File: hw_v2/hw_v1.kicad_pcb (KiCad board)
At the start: 4 copper layers, 190.1 x 116.5 mm, 501 parts, among them J1 Conn_02x24_Counter_Clockwise, J1 USB_B_Mini, J10 Conn_01x01, J11 Conn_01x01, J12 Conn_01x01, J12 Delphi_Sicma_24, J13 Conn_01x01, J13 Delphi_Sicma_24, J14 Conn_01x04, J15 Conn_01x01, J15 Conn_01x03, J16 47352-1001, J17 Conn_01x01, J19 Conn_01x06, J2 Conn_01x05, J2 Conn_02x05_Odd_Even, J3 Conn_01x01, J3 Conn_01x05, J4 Conn_01x05, J4 Conn_02x05_Counter_Clockwise, J5 Conn_01x01, J5 Conn_01x03, J6 Conn_01x04, J6 Micro_SD_Card_Det, J7 TC2030, J8 USB_B, J9 Tag connect, Q1 AO3400A, Q1 IPD30N06S2L-23, Q2 AO3400A, Q3 FDS6890A, Q4 SS8050, Q5 SS8050, Q6 AO3400A, Q7 AO3400A, SW1 SW_Push, SW2 SW_Push, SW3 SW_Push, SW4 SW_Push, U1 MCZ33810EK, U1 STM32F427VGT6, U10 BMP280, U10 VNLD5090, U11 L78M05ABDT-TR, U12 LM74800, U13 STM32F407VGTx, U14 TJA1051T-3, U15 25Q16, U16 REF3033, U17 SRV05-4, U18 VNLD5090, U19 L78M05ABDT-TR, U2 TC4424A, U2 TLE8888QK, U21 ADXL343, U3 TC4424A, U31 MIC4427, U32 MIC4427, U33 MIC4427, U35 MCP6004, U36 MCP6004, U4 MAX9926UAEE+, U4 TLE9201SG, U46 MCP6004, U5 LM1117-3.3, U5 TPL7407LAPWR, U6 LMV324, U7 LMV324, U7 XC6206 3.3V, U8 AMS1117-3.3, U8 MCP6004, U9 SP720ABTG, U9 VNLD5090, X1 8MHz 20pF, Y1 32.768kHz, Y2 25MHz, Y2 32768 Hz

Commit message: WIP v7
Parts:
- removed the C1 at (87.1, 63.7)
- removed the C1 at (318.1, 78.7)
- removed the C10 at (318.1, 117.7)
- removed the C10 at (49.3, 136.8)
- removed C11, C12, C13, C21, C22, C23: 100nF, Capacitor_SMD:C_0805_2012Metric
- removed C11: 4.7nF, Capacitor_SMD:C_0603_1608Metric
- removed C12: 1nF, Capacitor_SMD:C_0603_1608Metric
- removed C13, C17, C18, C24, C6, C78: 100nF, Capacitor_SMD:C_0603_1608Metric
- removed the C14 at (122.9, 95.6)
- removed the C14 at (325.8, 100.6)
- removed the C15 at (276.8, 63.4)
- removed the C15 at (122.7, 86.3)
- removed C16, C55, C56, C57, C59: 100nF, Capacitor_SMD:C_0402_1005Metric
- removed C16, C17, C18, C24, C27, C28: 0.22uF, Capacitor_SMD:C_0603_1608Metric
- removed the C19 at (105.0, 85.7)
- removed the C19 at (273.4, 63.1)
- removed the C2 at (311.7, 109.6)
- removed the C2 at (90.7, 59.5)
- removed C20: 0.1uF, Capacitor_SMD:C_0805_2012Metric
- removed C20, C79, C80, C82: 10nF, Capacitor_SMD:C_0603_1608Metric
- removed C21, C22: 18pF, Capacitor_SMD:C_0603_1608Metric
- removed C23, C27: 1uF, Capacitor_SMD:C_0603_1608Metric
- removed the C25 at (74.5, 116.7)
- removed the C25 at (298.9, 100.1)
- removed the C26 at (279.7, 96.0)
- removed the C26 at (109.5, 99.1)
- removed C28: 6.8pF, Capacitor_SMD:C_0603_1608Metric
- removed the C29 at (295.9, 117.2)
- removed the C29 at (91.1, 112.3)
- removed the C3 at (87.1, 59.5)
- removed the C3 at (314.3, 78.7)
- removed the C30 at (277.2, 112.6)
- removed the C30 at (115.1, 135.8)
- removed the C31 at (297.6, 112.6)
- removed the C31 at (103.3, 124.2)
- removed the C32 at (297.4, 100.1)
- removed the C32 at (120.6, 116.9)
- removed the C33 at (92.6, 113.8)
- removed the C33 at (279.7, 97.5)
- removed the C34 at (122.9, 126.6)
- removed the C34 at (259.2, 108.6)
- removed the C35 at (308.2, 61.6)
- removed the C35 at (104.9, 128.7)
- removed the C36 at (109.2, 124.8)
- removed the C36 at (261.5, 126.4)
- removed the C37 at (69.2, 81.7)
- removed the C37 at (298.2, 132.6)
- removed the C38 at (261.5, 124.9)
- removed the C38 at (117.9, 105.2)
- removed the C39 at (108.0, 97.6)
- removed the C39 at (260.6, 122.5)
- removed the C4 at (90.7, 63.7)
- removed the C4 at (305.2, 74.9)
- removed the C40 at (299.7, 80.1)
- removed the C40 at (110.8, 123.2)
- removed the C41 at (320.7, 100.6)
- removed the C41 at (112.5, 121.3)
- removed the C42 at (115.3, 115.1)
- removed the C42 at (301.3, 126.1)
- removed the C43 at (326.9, 97.3)
- removed the C43 at (116.7, 116.5)
- removed the C44 at (120.0, 119.0)
- removed the C44 at (283.3, 121.5)
- removed the C45 at (122.9, 124.6)
- removed the C45 at (303.0, 64.7)
- removed the C46 at (118.7, 124.8)
- removed the C46 at (301.1, 63.5)
- removed the C47 at (300.9, 64.7)
- removed the C47 at (96.8, 91.4)
- removed the C48 at (122.7, 99.0)
- removed the C48 at (299.0, 63.5)
- removed the C49 at (122.9, 108.2)
- removed the C49 at (298.5, 64.7)
- removed the C5 at (303.6, 74.9)
- removed the C5 at (85.1, 81.5)
- removed the C50 at (100.7, 89.3)
- removed the C50 at (296.8, 63.5)
- removed the C51 at (296.3, 64.7)
- removed the C51 at (126.4, 58.9)
- removed the C52 at (292.5, 66.7)
- removed the C52 at (130.2, 74.3)
- removed the C53 at (130.3, 59.0)
- removed the C53 at (292.0, 67.9)
- removed the C54 at (290.1, 66.7)
- removed the C54 at (127.8, 79.7)
- removed C55: 100uF ±20% 35V, Capacitor_SMD:CP_Elec_6.3x7.7
- removed C6: 0.01uF, Capacitor_SMD:C_0805_2012Metric
- removed the C7 at (304.3, 77.2)
- removed the C7 at (89.1, 92.8)
- removed the C8 at (318.1, 114.7)
- removed the C8 at (89.1, 95.4)
- removed the C9 at (122.5, 113.4)
- removed the C9 at (318.1, 116.2)
- removed Churrosoft: SYM_Hot_Large, OpenEFI-STM32F_rev3:churro_new_v4
- removed the D1 at (81.4, 53.1)
- removed the D1 at (329.0, 100.9)
- removed the D16 at (105.7, 87.9)
- removed the D16 at (294.7, 132.9)
- removed the D17 at (289.6, 125.6)
- removed the D17 at (113.3, 87.9)
- removed the D19 at (259.2, 107.0)
- removed the D19 at (90.1, 101.9)
- removed the D2 at (81.4, 62.6)
- removed the D2 at (319.5, 106.2)
- removed the D20 at (79.3, 123.8)
- removed the D20 at (322.9, 46.4)
- removed the D21 at (272.5, 117.7)
- removed the D21 at (79.3, 126.8)
- removed the D22 at (84.9, 140.0)
- removed the D22 at (272.5, 119.6)
- removed the D23 at (84.9, 143.2)
- removed the D23 at (272.5, 115.8)
- removed D27: LED-YELLOW, LED_SMD:LED_0805_2012Metric
- removed D27, D31, D32, D33, D34: 3.1v, Diode_SMD:D_SOD-323
- removed the D28 at (74.3, 66.1)
- removed the D28 at (298.2, 95.1)
- removed the D29 at (290.7, 93.7)
- removed the D29 at (49.6, 72.7)
- removed the D3 at (77.5, 44.2)
- removed the D3 at (269.5, 51.8)
- removed the D30 at (52.2, 75.1)
- removed the D30 at (328.4, 76.0)
- removed D31, D33, D35: LED-RED, LED_SMD:LED_0603_1608Metric
- removed D32, D34, D43: 1N4148WS, Diode_SMD:D_SOD-323
- removed D35: SM6T33A, Diode_SMD:D_SMB
- removed D36: SS54, Diode_SMD:D_SMA
- removed D38, D39, D40: SRV05-4, Package_TO_SOT_SMD:SOT-23-6
- removed the D4 at (81.4, 50.9)
- removed the D4 at (275.1, 51.9)
- removed D41: SM15T33C, Diode_SMD:D_SMC
- removed D42: BAV70, Package_TO_SOT_SMD:SOT-23
- removed the D5 at (81.4, 60.5)
- removed the D5 at (269.5, 48.2)
- removed the D6 at (77.5, 42.2)
- removed the D6 at (269.5, 44.7)
- removed the D7 at (81.4, 58.4)
- removed the D7 at (288.3, 129.1)
- removed F1: Polyfuse, Fuse:Fuse_1812_4532Metric
- removed FB1: FILTER, Resistor_SMD:R_0603_1608Metric_Pad1.05x0.95mm_HandSolder
- removed FID3, FID4, FID5, FID6: Fiducial, Fiducial:Fiducial_0.5mm_Mask1mm
- removed the G*** at (62.8, 113.8)
- removed the G*** at (96.8, 136.5)
- removed the J1 at (185.2, 125.3)
- removed J12: Delphi_Sicma_24, uEFI_v5:Delphi_Sicma_24_Grey
- removed J12, J13, J15 (x2), J17, J5: Conn_01x01, Connector_Pin:Pin_D0.7mm_L6.5mm_W1.8mm_FlatFork
- removed J13: Delphi_Sicma_24, uEFI_v5:Delphi_Sicma_24_Black
- removed J15, J5: Conn_01x03, Connector_PinHeader_2.54mm:PinHeader_1x03_P2.54mm_Vertical
- removed J19: Conn_01x06, Connector_JST:JST_EH_B5B-EH-A_1x05_P2.50mm_Vertical
- removed the J2 at (280.0, 129.6)
- removed the J2 at (39.2, 99.0)
- removed the J3 at (275.1, 57.0)
- removed the J3 at (86.0, 43.3)
- removed J4: Conn_01x05, Connector_PinHeader_2.54mm:PinHeader_1x05_P2.54mm_Vertical
- removed J4: Conn_02x05_Counter_Clockwise, Connector_PinHeader_2.54mm:PinHeader_2x05_P2.54mm_Vertical_SMD
- removed J6: Micro_SD_Card_Det, Connector_Card:microSD_HC_Molex_104031-0811
- removed J6: Conn_01x04, Connector_PinHeader_2.54mm:PinHeader_1x04_P2.54mm_Vertical
- removed J7: TC2030, Connector:Tag-Connect_TC2030-IDC-NL_2x03_P1.27mm_Vertical
- removed JP1: Jumper_3_Bridged12, Jumper:SolderJumper-3_P1.3mm_Bridged12_Pad1.0x1.5mm
- removed JP14: Jumper_2_Open, Jumper:SolderJumper-2_P1.3mm_Open_TrianglePad1.0x1.5mm
- removed the JP2 at (279.6, 82.2)
- removed the JP2 at (84.4, 69.1)
- removed JP4: SolderJumper_2_Open, Jumper:SolderJumper-2_P1.3mm_Open_RoundedPad1.0x1.5mm
- removed LOGO1: DNP, Symbol:OSHW-Logo2_7.3x6mm_SilkScreen
- removed LOGO3: LOGO, rusefi_lib:MRE_QR_code
- removed NT1: Net-Tie_2, rusEFI_Ola:Net-Tie_2_8.5mil
- removed NT2: Net-Tie_2, hw_microRusEfi-master:Net-Tie_2_8.5mil
- removed NT3: Analog Ground Net Tie, NetTie:NetTie-2_SMD_Pad0.5mm
- removed Q1: IPD30N06S2L-23, Package_TO_SOT_SMD:TO-252-2
- removed Q1, Q2: AO3400A, Package_TO_SOT_SMD:SOT-23
- removed Q3: FDS6890A, Package_SO:SOP-8_3.9x4.9mm_P1.27mm
- removed the R1 at (41.7, 66.3)
- removed the R1 at (273.9, 76.0)
- removed R10, R5: 10k, Resistor_SMD:R_0603_1608Metric
- removed R10: 1k, Resistor_SMD:R_1206_3216Metric
- removed the R11 at (287.4, 65.7)
- removed the R11 at (78.1, 83.5)
- removed R12, R13, R141, R39, R45, R46, R6, R60, R61, R62, R63, R70, R71, R76, R77, R78: 10K, Resistor_SMD:R_0603_1608Metric
- removed R12, R13, R18, R19, R20, R28, R29, R30: 470R, Resistor_SMD:R_0805_2012Metric
- removed R120, R121, R122, R123, R124, R125: 100, Resistor_SMD:R_1206_3216Metric
- removed R131, R24, R41, R52: 470K, Resistor_SMD:R_0402_1005Metric
- removed R139: 39k, Resistor_SMD:R_0603_1608Metric
- removed R14, R20, R23, R25: 2.7k, Resistor_SMD:R_0603_1608Metric
- removed R14, R15, R25: 2.49k +-1%, Resistor_SMD:R_0603_1608Metric
- removed R15, R17, R18, R19: DNP, Resistor_SMD:R_0603_1608Metric
- removed the R16 at (272.4, 76.0)
- removed the R16 at (74.5, 114.6)
- removed R17, R24, R33, R35, R36, R45, R46, R47: 180k, Resistor_SMD:R_0805_2012Metric
- removed the R2 at (308.9, 102.0)
- removed the R2 at (90.7, 57.4)
- removed R21: 604R, Resistor_SMD:R_0805_2012Metric
- removed R21, R30, R33, R8, R84, R85: 0R, Resistor_SMD:R_0603_1608Metric
- removed R22: 3.88k, Resistor_SMD:R_0603_1608Metric
- removed R22: 120, Resistor_SMD:R_0805_2012Metric
- removed R23, R26, R39, R40, R41, R50, R51, R52: 348k, Resistor_SMD:R_0805_2012Metric
- removed R26, R35, R5, R59, R64, R65, R66, R67, R72, R73, R74: 6.8K, Resistor_SMD:R_0603_1608Metric
- removed the R27 at (98.7, 121.3)
- removed the R27 at (288.1, 63.0)
- removed R28, R48: 2.2k, Resistor_SMD:R_0603_1608Metric
- removed R29, R36, R48, R49 (x2), R50, R51, R59, R6, R60, R61, R66, R9: 1k, Resistor_SMD:R_0603_1608Metric
- removed the R3 at (87.1, 61.6)
- removed the R3 at (307.2, 80.4)
- removed the R31 at (116.4, 48.5)
- removed the R31 at (297.3, 51.5)
- removed the R32 at (293.2, 88.1)
- removed the R32 at (87.5, 123.9)
- removed the R34 at (297.0, 56.5)
- removed the R34 at (87.5, 127.0)
- removed the R37 at (87.7, 135.6)
- removed the R37 at (296.6, 54.1)
- removed the R38 at (296.2, 91.1)
- removed the R38 at (89.4, 135.6)
- removed the R4 at (307.6, 97.4)
- removed the R4 at (90.7, 61.6)
- removed R40: DNP, Resistor_SMD:R_0402_1005Metric
- removed the R42 at (83.0, 130.1)
- removed the R42 at (273.4, 61.6)
- removed the R43 at (83.0, 132.9)
- removed the R43 at (271.0, 130.5)
- removed the R44 at (293.2, 91.1)
- removed the R44 at (83.0, 135.7)
- removed R47: 100K, Resistor_SMD:R_0603_1608Metric
- removed the R53 at (74.6, 69.6)
- removed the R53 at (302.2, 88.1)
- removed the R54 at (77.4, 62.7)
- removed the R54 at (302.8, 56.8)
- removed the R55 at (300.7, 88.1)
- removed the R55 at (54.8, 83.7)
- removed the R56 at (299.2, 51.5)
- removed the R56 at (54.8, 77.9)
- removed the R57 at (299.2, 88.1)
- removed the R57 at (54.8, 79.9)
- removed the R58 at (54.8, 82.0)
- removed the R58 at (299.5, 56.5)
- removed R62: 48.7k, Resistor_SMD:R_0603_1608Metric
- removed R63: 42.2k, Resistor_SMD:R_0603_1608Metric
- removed R64: 9.09k, Resistor_SMD:R_0603_1608Metric
- removed R65: 3.48k, Resistor_SMD:R_0603_1608Metric
- removed R67: 100R, Resistor_SMD:R_0603_1608Metric
- removed the R68 at (290.2, 91.1)
- removed the R68 at (93.0, 36.1)
- removed the R69 at (93.0, 39.2)
- removed the R69 at (288.7, 91.1)
- removed the R7 at (304.6, 59.4)
- removed the R7 at (85.1, 78.0)
- removed R8: 4.99K 1/2W, Resistor_SMD:R_0805_2012Metric
- removed R83, R9: 4.7K, Resistor_SMD:R_0603_1608Metric
- removed R86: 0R, Resistor_SMD:R_0805_2012Metric
- removed REF** (x4): MountingHole_3.2mm_M3_ISO14580_Pad, MountingHole:MountingHole_3.2mm_M3_ISO14580_Pad
- removed the RN1 at (77.7, 51.5)
- removed the RN1 at (268.9, 116.3)
- removed RN13: 10k, Resistor_SMD:R_Array_Convex_4x0603
- removed the RN2 at (77.5, 59.4)
- removed the RN2 at (302.1, 60.8)
- removed the RN3 at (101.2, 128.0)
- removed the RN3 at (291.5, 63.6)
- removed SW1: SW_Push, Button_Switch_SMD:SW_SPST_CK_RS282G05A3
- removed the SW2 at (118.5, 140.0)
- removed the SW2 at (270.5, 104.8)
- removed SW3, SW4: SW_Push, Button_Switch_SMD:SW_Push_SPST_NO_Alps_SKRK
- removed TP0: GND, TestPoint:TestPoint_Pad_D2.0mm
- removed the TP1 at (90.5, 57.4)
- removed the TP1 at (281.7, 87.9)
- removed TP10, TP11, TP14, TP15, TP16, TP17, TP18, TP19, TP20, TP9: TestPoint_Alt, TestPoint:TestPoint_THTPad_1.0x1.0mm_Drill0.5mm
- removed the TP12 at (258.4, 91.8)
- removed the TP12 at (73.2, 84.6)
- removed the TP2 at (287.6, 94.9)
- removed the TP2 at (83.3, 90.5)
- removed the TP3 at (258.4, 100.9)
- removed the TP3 at (88.0, 84.6)
- removed the TP4 at (301.3, 94.3)
- removed the TP4 at (83.2, 86.1)
- removed the TP5 at (258.4, 97.9)
- removed the TP5 at (79.6, 85.3)
- removed U1: STM32F427VGT6, Package_QFP:LQFP-100_14x14mm_P0.5mm
- removed U1: MCZ33810EK, uEFI_v5:SOP65P1030X245-33N
- removed the U10 at (319.9, 71.0)
- removed the U10 at (100.8, 86.0)
- removed the U2 at (317.3, 89.1)
- removed U31, U32, U33: MIC4427, Package_SO:SOIC-8_3.9x4.9mm_P1.27mm
- removed U35, U36, U46: MCP6004, Package_SO:TSSOP-14_4.4x5mm_P0.65mm
- removed U4: MAX9926UAEE+, Package_SO:QSOP-16_3.9x4.9mm_P0.635mm
- removed U4: TLE9201SG, Package_SO:Infineon_PG-DSO-12-11
- removed the U5 at (261.4, 116.6)
- removed the U5 at (64.6, 70.6)
- removed the U7 at (304.7, 113.0)
- removed the U7 at (98.5, 79.3)
- removed the U8 at (298.6, 83.7)
- removed the U8 at (128.1, 114.4)
- removed the U9 at (98.6, 62.5)
- removed the U9 at (314.3, 71.0)
- removed X1: 8MHz 20pF, Crystal:Crystal_SMD_5032-2Pin_5.0x3.2mm
- removed the Y2 at (114.9, 119.7)
- removed the Y2 at (282.1, 118.8)
- added C1: 0.01uF, Capacitor_SMD:C_0805_2012Metric, F.Cu at (223.8, 129.2)
- added C10: 100uF ±20% 35V, Capacitor_SMD:CP_Elec_6.3x7.7, F.Cu at (226.7, 91.4)
- added C14: 100nF, Capacitor_SMD:C_0805_2012Metric, F.Cu at (210.3, 105.7)
- added C15: 47nF, Capacitor_SMD:C_0603_1608Metric, F.Cu at (201.5, 102.4)
- added C19: 100nF, Capacitor_SMD:C_0402_1005Metric, F.Cu at (239.8, 102.2)
- added C2: 0.01uF, Capacitor_SMD:C_0805_2012Metric, F.Cu at (223.8, 132.2)
- added C25: 100nF, Capacitor_SMD:C_0402_1005Metric, F.Cu at (239.8, 104.1)
- added C26: 2.2uF, Capacitor_SMD:C_0805_2012Metric, F.Cu at (194.0, 66.9)
- added C29: 2.2uF, Capacitor_SMD:C_0805_2012Metric, F.Cu at (194.0, 69.9)
- added C3: 10nF, Capacitor_SMD:C_0603_1608Metric, F.Cu at (219.6, 128.9)
- added C30: 100nF, Capacitor_SMD:C_0805_2012Metric, F.Cu at (194.0, 73.0)
- added C31: 100nF, Capacitor_SMD:C_0805_2012Metric, F.Cu at (194.0, 76.0)
- added C32: 100nF, Capacitor_SMD:C_0805_2012Metric, F.Cu at (194.0, 79.0)
- added C33: 100nF, Capacitor_SMD:C_0805_2012Metric, F.Cu at (194.0, 82.0)
- added C34: 1uF, Capacitor_SMD:C_0805_2012Metric, F.Cu at (194.0, 85.0)
- added C35: 100nF, Capacitor_SMD:C_0805_2012Metric, F.Cu at (198.4, 66.9)
- added C36: 100nF, Capacitor_SMD:C_0805_2012Metric, F.Cu at (198.4, 69.9)
- added C37: 100nF, Capacitor_SMD:C_0805_2012Metric, F.Cu at (198.4, 73.0)
- added C38: 4.7uF, Capacitor_SMD:C_0805_2012Metric, F.Cu at (198.4, 76.0)
- added C39: 100nF, Capacitor_SMD:C_0805_2012Metric, F.Cu at (198.4, 79.0)
- added C4: 10nF, Capacitor_SMD:C_0603_1608Metric, F.Cu at (219.6, 131.4)
- added C40: 6.8pF, Capacitor_SMD:C_0805_2012Metric, F.Cu at (198.4, 82.0)
- added C41: 6.8pF, Capacitor_SMD:C_0805_2012Metric, F.Cu at (198.4, 85.0)
- added C42: 15pF, Capacitor_SMD:C_0805_2012Metric, F.Cu at (202.9, 66.9)
- added C43: 15pF, Capacitor_SMD:C_0805_2012Metric, F.Cu at (202.9, 69.9)
- added C44: 1u, Capacitor_SMD:C_0805_2012Metric, F.Cu at (202.9, 73.0)
- added C45: 1u, Capacitor_SMD:C_0805_2012Metric, F.Cu at (202.9, 76.0)
- added C46: 100n, Capacitor_SMD:C_0805_2012Metric, F.Cu at (202.9, 79.0)
- added C47: 100nF, Capacitor_SMD:C_0805_2012Metric, F.Cu at (224.4, 120.2)
- added C48: 47nF, Capacitor_SMD:C_0603_1608Metric, F.Cu at (201.5, 104.9)
- added C49: 100nF, Capacitor_SMD:C_0805_2012Metric, F.Cu at (210.3, 108.7)
- added C5: 0.01uF, Capacitor_SMD:C_0805_2012Metric, F.Cu at (223.8, 135.2)
- added C50: 100nF, Capacitor_SMD:C_0805_2012Metric, F.Cu at (224.4, 123.3)
- added C51: 10nF, Capacitor_SMD:C_0603_1608Metric, F.Cu at (201.5, 107.5)
- added C52: 10nF, Capacitor_SMD:C_0603_1608Metric, F.Cu at (201.5, 110.0)
- added C53: 10nF, Capacitor_SMD:C_0603_1608Metric, F.Cu at (201.5, 112.5)
- added C54: 10nF, Capacitor_SMD:C_0603_1608Metric, F.Cu at (201.5, 115.0)
- added C60: 100nF, Capacitor_SMD:C_0402_1005Metric, F.Cu at (239.8, 108.1)
- added C63: 10nF, Capacitor_SMD:C_0603_1608Metric, F.Cu at (219.6, 102.4)
- added C64: 100nF, Capacitor_SMD:C_0402_1005Metric, F.Cu at (239.8, 110.0)
- added C66: 100nF, Capacitor_SMD:C_0402_1005Metric, F.Cu at (239.8, 112.0)
- added C68: 10nF, Capacitor_SMD:C_0603_1608Metric, F.Cu at (219.6, 104.9)
- added C69: 100uF ±20% 35V, Capacitor_SMD:CP_Elec_6.3x7.7, F.Cu at (204.7, 128.1)
- added C7: 0.01uF, Capacitor_SMD:C_0805_2012Metric, F.Cu at (223.8, 138.2)
- added C8: 4.7nF, Capacitor_SMD:C_0805_2012Metric, F.Cu at (223.8, 141.2)
- added C9: 100nF, Capacitor_SMD:C_0805_2012Metric, F.Cu at (210.3, 102.7)
- added D1: LED, LED_SMD:LED_0805_2012Metric, F.Cu at (249.8, 102.7)
- added D16: SRV05-4, Package_TO_SOT_SMD:SOT-23-6, F.Cu at (240.6, 121.3)
- added D17: SS54, Diode_SMD:D_SMA, F.Cu at (191.4, 128.2)
- added D19: 1N5819WS, Diode_SMD:D_SOD-323_HandSoldering, F.Cu at (197.4, 97.5)
- added D2: LED, LED_SMD:LED_0805_2012Metric, F.Cu at (249.8, 105.7)
- added D20: LED, LED_SMD:LED_0805_2012Metric, F.Cu at (189.5, 66.9)
- added D21: LED, LED_SMD:LED_0805_2012Metric, F.Cu at (189.5, 70.0)
- added D22: LED, LED_SMD:LED_0805_2012Metric, F.Cu at (189.5, 73.0)
- added D23: LED, LED_SMD:LED_0805_2012Metric, F.Cu at (189.5, 76.1)
- added D28: MM3Z24VT1G, Diode_SMD:D_SOD-323, F.Cu at (234.1, 95.5)
- added D29: S110FA, Diode_SMD:D_SOD-123F, F.Cu at (234.7, 89.0)
- added D3: 1N5819WS, Diode_SMD:D_SOD-323_HandSoldering, F.Cu at (263.0, 102.7)
- added D30: S110FA, Diode_SMD:D_SOD-123F, F.Cu at (234.7, 92.3)
- added D4: LED, LED_SMD:LED_0805_2012Metric, F.Cu at (249.8, 108.8)
- added D5: LED, LED_SMD:LED_0805_2012Metric, F.Cu at (249.8, 111.8)
- added D6: 1N5819WS, Diode_SMD:D_SOD-323_HandSoldering, F.Cu at (263.0, 105.6)
- added D7: LED, LED_SMD:LED_0805_2012Metric, F.Cu at (249.8, 114.9)
- added FID2: Fiducial, Fiducial:Fiducial_0.5mm_Mask1mm, F.Cu at (227.9, 122.6)
- added J2: Conn_01x01, TestPoint:TestPoint_THTPad_2.0x2.0mm_Drill1.0mm, F.Cu at (249.2, 67.5)
- added J3: Conn_01x01, TestPoint:TestPoint_THTPad_2.0x2.0mm_Drill1.0mm, F.Cu at (249.2, 71.5)
- added JP2: Jumper_3_Bridged12, Jumper:SolderJumper-3_P1.3mm_Bridged12_Pad1.0x1.5mm, F.Cu at (233.1, 140.1)
- added R1: 2.2k, Resistor_SMD:R_0603_1608Metric, F.Cu at (219.6, 133.9)
- added R100: 10K, Resistor_SMD:R_0603_1608Metric, F.Cu at (223.6, 115.0)
- added R101: 39k, Resistor_SMD:R_0603_1608Metric, F.Cu at (223.6, 117.5)
- added R102: 6.8K, Resistor_SMD:R_0603_1608Metric, F.Cu at (227.6, 102.4)
- added R104: 6.8K, Resistor_SMD:R_0603_1608Metric, F.Cu at (227.6, 104.9)
- added R106: 10K, Resistor_SMD:R_0603_1608Metric, F.Cu at (227.6, 107.5)
- added R108: 10K, Resistor_SMD:R_0603_1608Metric, F.Cu at (227.6, 110.0)
- added R11: 10k, Resistor_SMD:R_0603_1608Metric, F.Cu at (219.6, 144.0)
- added R16: 2.7k, Resistor_SMD:R_0603_1608Metric, F.Cu at (219.6, 107.5)
- added R2: 10k, Resistor_SMD:R_0603_1608Metric, F.Cu at (219.6, 136.4)
- added R27: 10k, Resistor_SMD:R_0603_1608Metric, F.Cu at (207.1, 66.7)
- added R3: 10k, Resistor_SMD:R_0603_1608Metric, F.Cu at (219.6, 138.9)
- added R31: 120R, Resistor_SMD:R_1206_3216Metric, F.Cu at (207.9, 96.7)
- added R32: 4.7k, Resistor_SMD:R_0603_1608Metric, F.Cu at (207.1, 69.2)
- added R34: 4.7k, Resistor_SMD:R_0603_1608Metric, F.Cu at (207.1, 71.7)
- added R37: 4.7k, Resistor_SMD:R_0603_1608Metric, F.Cu at (207.1, 74.2)
- added R38: 4.7k, Resistor_SMD:R_0603_1608Metric, F.Cu at (207.1, 76.7)
- added R4: 2.2k, Resistor_SMD:R_0603_1608Metric, F.Cu at (219.6, 141.5)
- added R42: 4.7k, Resistor_SMD:R_0603_1608Metric, F.Cu at (207.1, 79.2)
- added R43: 4.7k, Resistor_SMD:R_0603_1608Metric, F.Cu at (207.1, 81.7)
- added R44: 4.7k, Resistor_SMD:R_0603_1608Metric, F.Cu at (207.1, 84.2)
- added R53: 1k, Resistor_SMD:R_0603_1608Metric, F.Cu at (240.3, 66.7)
- added R54: 100k, Resistor_SMD:R_0603_1608Metric, F.Cu at (240.3, 69.2)
- added R55: 100k, Resistor_SMD:R_0603_1608Metric, F.Cu at (240.3, 71.7)
- added R56: 100k, Resistor_SMD:R_0603_1608Metric, F.Cu at (240.3, 74.2)
- added R57: 1k, Resistor_SMD:R_0603_1608Metric, F.Cu at (240.3, 76.7)
- added R58: 1k, Resistor_SMD:R_0603_1608Metric, F.Cu at (240.3, 79.2)
- added R68: 1k, Resistor_SMD:R_0603_1608Metric, F.Cu at (240.3, 81.7)
- added R69: 100k, Resistor_SMD:R_0603_1608Metric, F.Cu at (240.3, 84.2)
- added R7: 4.99K 1/2W, Resistor_SMD:R_0805_2012Metric, F.Cu at (232.5, 143.6)
- added R91: 10K, Resistor_SMD:R_0603_1608Metric, F.Cu at (223.6, 104.9)
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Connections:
- A1 pad 8: +12V -> HEATER+
- C58 pad 1: Net-(C58-Pad1) -> Net-(RN4-R3.2)
- D13 pad 2: GND -> +5C
- D14 pad 1: Net-(D14-Pad1) -> Net-(RN4-R4.2)
- D14 pad 2: /MCU/PA9 -> GND
- D15 pad 1: /12V_MREL -> Net-(D15-K)
- D15 pad 2: /LS1 -> +5C
- D37 pad 1: /12V_SAFE -> HEATER+
- D37 pad 2: /12V_KEY -> GND
- J1 pad 1: unconnected-(J1-Pin_1-Pad1) -> +12VA
- J1 pad 10: unconnected-(J1-Pin_10-Pad10) -> SW_TABLE
- J1 pad 11: unconnected-(J1-Pin_11-Pad11) -> SW_SHIFT
- J1 pad 12: unconnected-(J1-Pin_12-Pad12) -> SW_AC
- J1 pad 13: unconnected-(J1-Pin_13-Pad13) -> CAN-
- J1 pad 14: unconnected-(J1-Pin_14-Pad14) -> CAN+
- J1 pad 15: unconnected-(J1-Pin_15-Pad15) -> USB_D-
- J1 pad 16: unconnected-(J1-Pin_16-Pad16) -> USB_D+
- J1 pad 17: unconnected-(J1-Pin_17-Pad17) -> CLT_Sensor
- J1 pad 18: unconnected-(J1-Pin_18-Pad18) -> IAT_Sensor
- J1 pad 19: unconnected-(J1-Pin_19-Pad19) -> O2_Sensor
- J1 pad 2: unconnected-(J1-Pin_2-Pad2) -> HEATER+
- J1 pad 20: unconnected-(J1-Pin_20-Pad20) -> TPS_Sensor
- J1 pad 21: unconnected-(J1-Pin_21-Pad21) -> MAP_Sensor
- J1 pad 22: unconnected-(J1-Pin_22-Pad22) -> GNDREF
- J1 pad 23: unconnected-(J1-Pin_23-Pad23) -> LSU_ip
- J1 pad 24: unconnected-(J1-Pin_24-Pad24) -> LSU_vm
- J1 pad 25: unconnected-(J1-Pin_25-Pad25) -> LSU_rtrim
- J1 pad 26: unconnected-(J1-Pin_26-Pad26) -> LSU_un
- J1 pad 27: unconnected-(J1-Pin_27-Pad27) -> SPARE2_out
- J1 pad 28: unconnected-(J1-Pin_28-Pad28) -> SPARE1_out
- J1 pad 29: unconnected-(J1-Pin_29-Pad29) -> CEL-OUT
- J1 pad 3: unconnected-(J1-Pin_3-Pad3) -> HEATER-
- J1 pad 30: unconnected-(J1-Pin_30-Pad30) -> FAN-OUT
- J1 pad 31: unconnected-(J1-Pin_31-Pad31) -> FUELPUMP-OUT
- J1 pad 32: unconnected-(J1-Pin_32-Pad32) -> TACHO-OUT
- J1 pad 33: unconnected-(J1-Pin_33-Pad33) -> CAM+
- J1 pad 35: unconnected-(J1-Pin_35-Pad35) -> CRANK+
- J1 pad 36: unconnected-(J1-Pin_36-Pad36) -> CRANK-
- J1 pad 37: unconnected-(J1-Pin_37-Pad37) -> STEP-B2
- J1 pad 38: unconnected-(J1-Pin_38-Pad38) -> STEP-B1
- J1 pad 39: unconnected-(J1-Pin_39-Pad39) -> STEP-A1
- J1 pad 4: unconnected-(J1-Pin_4-Pad4) -> BOOST-OUT
- J1 pad 40: unconnected-(J1-Pin_40-Pad40) -> STEP-A2
- J1 pad 41: unconnected-(J1-Pin_41-Pad41) -> INJ-1-OUT
- J1 pad 42: unconnected-(J1-Pin_42-Pad42) -> INJ-2-OUT
- J1 pad 43: unconnected-(J1-Pin_43-Pad43) -> INJ-3-OUT
- J1 pad 44: unconnected-(J1-Pin_44-Pad44) -> INJ-4-OUT
- J1 pad 45: unconnected-(J1-Pin_45-Pad45) -> IGN-4-OUT
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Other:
- board size 190.1 x 116.5 mm -> 80.6 x 93.7 mm
- board text removed: "+12V"
- board text removed: "+5V"
- board text removed: "3V"
- board text removed: "5V"
- board text removed: "AUX_IN0"
- board text removed: "AUX_IN1"
- board text removed: "BT"
- board text removed: "CAN"
- board text removed: "CAN_R"
- board text removed: "CKP"
- board text removed: "CLT"
- board text removed: "CMP"
- board text removed: "Diseñado en Argentina"
- board text removed: "EXT O2"
- board text removed: "HALL"
- board text removed: "IAT"
- board text removed: "Ignición"
- board text removed: "In case of poor signal, short"
- board text removed: "Inyección"
- board text removed: "L0"
- board text removed: "L1"
- board text removed: "L2"
- board text removed: "MAP"
- board text removed: "MCU +5V"
- board text removed: "POWER"
- board text removed: "REV 2"
- board text removed: "RTC BATT"
- board text removed: "RX"
- board text removed: "Sensors +5V"
- board text removed: "TPS"
- board text removed: "TX"
- board text removed: "VBAT"
- board text removed: "VR"
- board text removed: "surge protection"
- board text removed: "uEFI v6"
- board text removed: "®"

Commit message: hw v2
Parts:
- removed D28: MM3Z24VT1G, Diode_SMD:D_SOD-323
- removed J10, J11, J2, J3: Conn_01x01, TestPoint:TestPoint_THTPad_2.0x2.0mm_Drill1.0mm
- removed Q4, Q5: SS8050, Package_TO_SOT_SMD:SOT-23
- removed Q6, Q7: AO3400A, Package_TO_SOT_SMD:SOT-23
- removed R53, R68: 1k, Resistor_SMD:R_0603_1608Metric
- removed R54, R69: 100k, Resistor_SMD:R_0603_1608Metric
- added C6: 100nF, Capacitor_SMD:C_0805_2012Metric, F.Cu at (191.6, 62.1)
- added R5: 4.7k, Resistor_SMD:R_0603_1608Metric, F.Cu at (232.0, 129.9)
- added R6: 4.7k, Resistor_SMD:R_0603_1608Metric, F.Cu at (232.0, 132.4)
- added R8: 4.7k, Resistor_SMD:R_0603_1608Metric, F.Cu at (232.0, 135.0)
- added R9: 4.7k, Resistor_SMD:R_0603_1608Metric, F.Cu at (232.0, 137.5)
- added SW1: SW_Push, Button_Switch_SMD:SW_SPST_CK_RS282G05A3, F.Cu at (215.0, 63.0)
- added TP10: TestPoint_Alt, TestPoint:TestPoint_Pad_1.0x1.0mm, F.Cu at (177.2, 56.5)
- added TP11: TestPoint_Alt, TestPoint:TestPoint_Pad_1.0x1.0mm, F.Cu at (180.3, 53.4)
- added TP14: TestPoint_Alt, TestPoint:TestPoint_Pad_1.0x1.0mm, F.Cu at (180.3, 56.5)
- added TP15: TestPoint_Alt, TestPoint:TestPoint_Pad_1.0x1.0mm, F.Cu at (183.3, 53.4)
- added TP16: TestPoint_Alt, TestPoint:TestPoint_Pad_1.0x1.0mm, F.Cu at (183.3, 56.5)
- added TP17: TestPoint_Alt, TestPoint:TestPoint_Pad_1.0x1.0mm, F.Cu at (186.4, 53.4)
- added TP18: TestPoint_Alt, TestPoint:TestPoint_Pad_1.0x1.0mm, F.Cu at (186.4, 56.5)
- added TP19: TestPoint_Alt, TestPoint:TestPoint_Pad_1.0x1.0mm, F.Cu at (177.2, 61.5)
- added TP9: TestPoint_Alt, TestPoint:TestPoint_Pad_1.0x1.0mm, F.Cu at (177.2, 53.4)
- added U1: MAX9924UAUB_, Package_SO:MSOP-10_3x3mm_P0.5mm, F.Cu at (201.3, 139.6)
- added U26: 74LVC2G17, Package_TO_SOT_SMD:SOT-363_SC-70-6, F.Cu at (200.9, 111.3)
- added U4: ~, hw_v2lib:WBO-module, F.Cu at (111.3, 80.7)
- SW2: footprint Button_Switch_SMD:SW_SPST_TL3342 -> Button_Switch_SMD:SW_SPST_CK_RS282G05A3
- moved U2 31.8 mm to (83.9, 104.5)
- moved U3 31.8 mm to (90.7, 104.5)
- moved BT1 29.4 mm to (180.5, 27.0)
- moved C10 13.2 mm to (213.5, 90.8)
- moved C14 13.2 mm to (197.2, 105.2)
- moved C15 13.2 mm to (188.3, 101.9)
- moved C3 13.2 mm to (206.4, 128.4)
- moved C35 13.2 mm to (185.2, 66.4)
- moved C36 13.2 mm to (185.2, 69.4)
- moved C37 13.2 mm to (185.2, 72.4)
- moved C38 13.2 mm to (185.2, 75.4)
- moved C39 13.2 mm to (185.2, 78.4)
- moved C4 13.2 mm to (206.4, 130.9)
- moved C40 13.2 mm to (185.2, 81.5)
- moved C41 13.2 mm to (185.2, 84.5)
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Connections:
- RN5 pad 1: +5C -> unconnected-(RN5-R1.1-Pad1)
- RN5 pad 3: +5C -> unconnected-(RN5-R3.1-Pad3)
- U13 pad 31: /EXT_0 -> unconnected-(U13-PA6-Pad31)
- U13 pad 32: /EXT_1 -> unconnected-(U13-PA7-Pad32)
- U13 pad 35: MCU-D0 -> unconnected-(U13-PB0-Pad35)
- U13 pad 36: MCU-D1 -> unconnected-(U13-PB1-Pad36)
- U13 pad 48: /PMIC1_CS -> unconnected-(U13-PB11-Pad48)
- U13 pad 51: /PMIC1_ENABLE -> unconnected-(U13-PB12-Pad51)
- U5 pad 10: Net-(J11-Pin_1) -> CEL-OUT
- U5 pad 11: Net-(J11-Pin_1) -> CEL-OUT
- U5 pad 12: Net-(J3-Pin_1) -> TACHO-OUT
- U5 pad 13: Net-(J3-Pin_1) -> TACHO-OUT
- U5 pad 4: Net-(J2-Pin_1) -> /RPM_OUT
- U5 pad 5: Net-(J2-Pin_1) -> /RPM_OUT
- U5 pad 6: Net-(J10-Pin_1) -> /CEL_OUT
- U5 pad 7: Net-(J10-Pin_1) -> /CEL_OUT
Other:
- board text added: "no recuerdo si este es el footprint correcto para este conector"

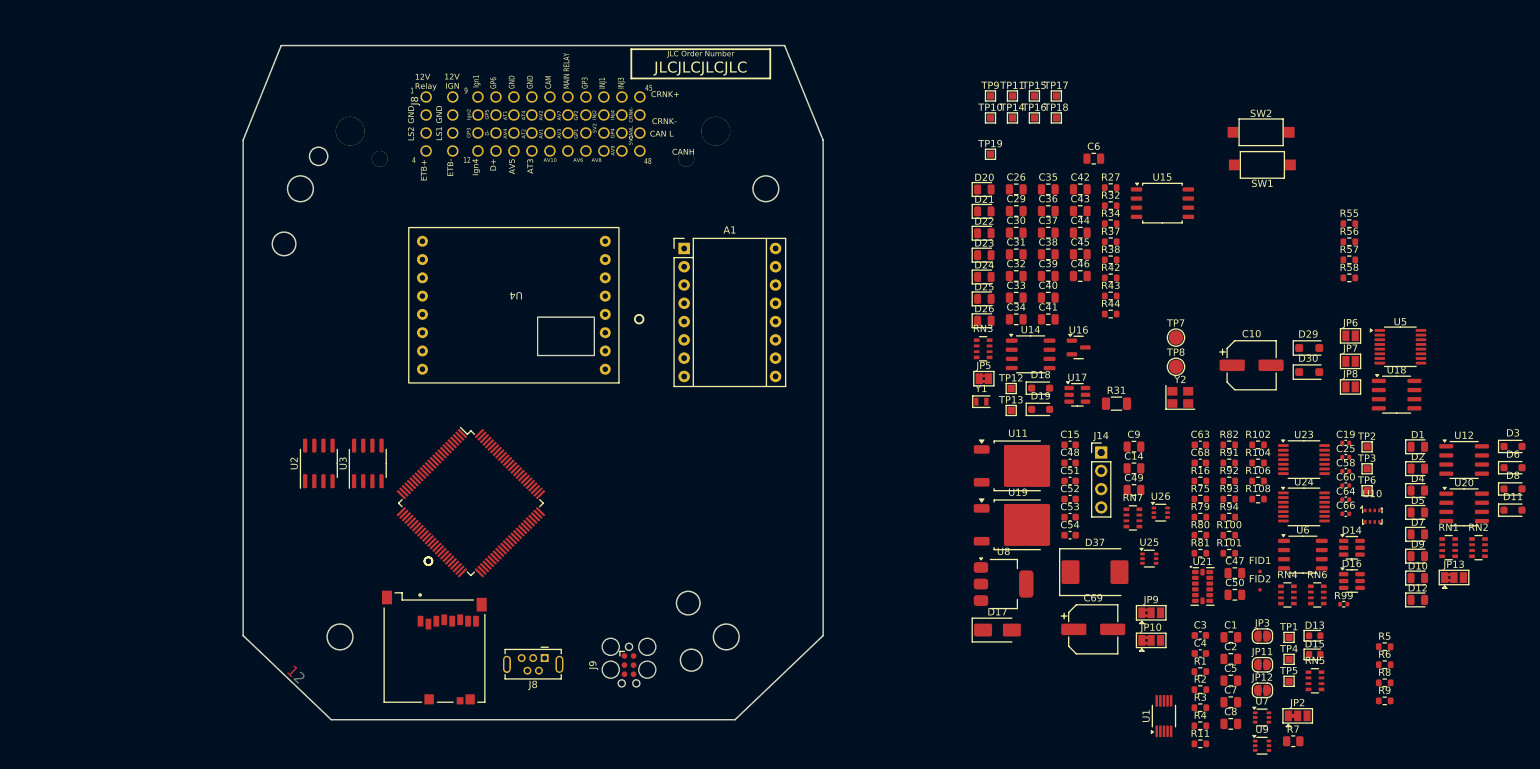
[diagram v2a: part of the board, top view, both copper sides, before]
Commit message: fix LCSC codes
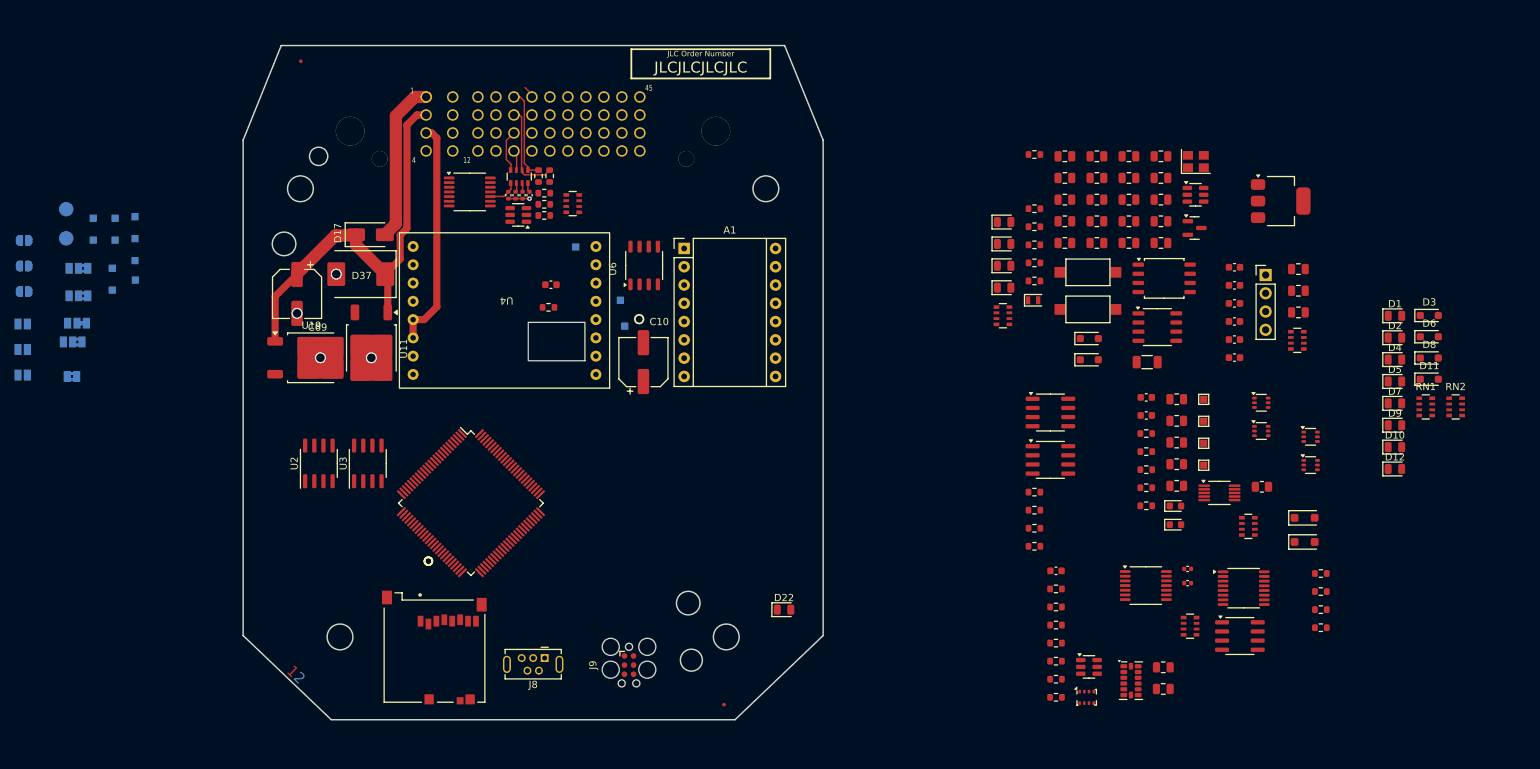
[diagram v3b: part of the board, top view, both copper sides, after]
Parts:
- removed D20, D21: LED, LED_SMD:LED_0805_2012Metric
- removed R32, R34: 4.7k, Resistor_SMD:R_0603_1608Metric
- removed R91, R92, R93, R94: 10K, Resistor_SMD:R_0603_1608Metric
- added RN8: 10k, Resistor_SMD:R_Array_Convex_4x0603, F.Cu at (119.2, 68.4)
- JP10, JP11, JP12, JP13, JP2, JP3, JP5, JP6, JP7, JP8, JP9, TP10, TP11, TP12, TP13, TP14, TP15, TP16, TP17, TP18, TP2, TP3, TP6, TP7, TP8, TP9: moved to B.Cu
- R99: footprint Resistor_SMD:R_0402_1005Metric -> Resistor_SMD:R_0603_1608Metric
- moved JP13 194.7 mm to (49.7, 87.6), turned to 180 degrees
- moved JP6 184.5 mm to (42.8, 85.1), turned to 180 degrees
- moved JP7 184.5 mm to (42.8, 88.7), turned to 180 degrees
- moved JP8 184.5 mm to (42.8, 92.2), turned to 180 degrees
- moved JP11 180.8 mm to (43.0, 77.0), turned to 180 degrees
- moved JP12 180.8 mm to (43.0, 80.6), turned to 180 degrees
- moved JP3 180.6 mm to (43.0, 73.5), turned to 180 degrees
- moved JP2 178.2 mm to (50.3, 85.0), turned to 180 degrees
- moved JP10 156.5 mm to (50.5, 81.2), turned to 180 degrees
- moved JP9 156.5 mm to (50.5, 77.4), turned to 180 degrees
- moved TP7 155.2 mm to (48.8, 69.2), turned to 180 degrees
- moved TP8 155.2 mm to (48.8, 73.2), turned to 180 degrees
- moved FID1 151.0 mm to (81.4, 48.6)
- moved TP17 129.5 mm to (58.4, 73.2), turned to 180 degrees
- moved TP18 129.5 mm to (58.4, 76.3), turned to 180 degrees
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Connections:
- J1 pad 19: O2_Sensor -> MAP_Sensor
- J1 pad 21: MAP_Sensor -> O2_Sensor
- R101 pad 2: /Sensors/12V -> HEATER+
- R102 pad 1: /Sensors/AV5_MCU -> /O2
- R104 pad 1: /Sensors/Vbat_MCU -> /VBATT
- R106 pad 2: /Sensors/AV5_MCU -> /O2
- R108 pad 2: /Sensors/Vbat_MCU -> /VBATT
- R16 pad 1: /Sensors/CLT_Sensor -> CLT_Sensor
- R75 pad 1: /Sensors/IAT_Sensor -> IAT_Sensor
- R79 pad 1: /Sensors/AT4_MCU -> /CLT
- R80 pad 1: /Sensors/AT3_MCU -> /IAT
- R81 pad 1: /Sensors/AT2_MCU -> /TPS
- R82 pad 1: /Sensors/AT1_MCU -> /MAP
- R99 pad 1: /Sensors/O2_Sensor -> O2_Sensor
- RN4 pad 1: /Sensors/CLT_Sensor -> CLT_Sensor
- RN4 pad 2: /Sensors/IAT_Sensor -> IAT_Sensor
- RN4 pad 3: /Sensors/TPS_Sensor -> TPS_Sensor
- RN4 pad 4: /Sensors/MAP_Sensor -> MAP_Sensor
- RN6 pad 1: /Sensors/O2_Sensor -> O2_Sensor
- TP10 pad 1: /Sensors/AT3_MCU -> /IAT
- TP11 pad 1: /Sensors/AT2_MCU -> /TPS
- TP14 pad 1: /Sensors/AT1_MCU -> /MAP
- TP15 pad 1: /Sensors/Vbat_MCU -> /VBATT
- TP16 pad 1: /Sensors/AV5_MCU -> /O2
- TP9 pad 1: /Sensors/AT4_MCU -> /CLT
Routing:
- net HEATER+: track 0.00 -> 58.9 mm
- net HEATER-: track 0.00 -> 31.8 mm
- net +12VA: track 0.00 -> 22.4 mm
- net IAT_Sensor: track 0.00 -> 13.7 mm
- net CLT_Sensor: track 0.00 -> 13.0 mm
- net MAP_Sensor: track 0.00 -> 5.89 mm
- net Net-(RN4-R4.2): track 0.00 -> 4.15 mm
- net GND: track 0.00 -> 2.94 mm, vias 0 -> 5
- net TPS_Sensor: track 0.00 -> 2.85 mm
- net O2_Sensor: track 0.00 -> 1.71 mm
- net Net-(RN4-R1.2): track 0.00 -> 1.31 mm
- net Net-(RN4-R3.2): track 0.00 -> 1.29 mm
- net Net-(RN4-R2.2): track 0.00 -> 1.23 mm
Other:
- rule pad_to_mask_clearance: 0 -> 0.000076

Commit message: wip analog frontend & power
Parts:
- added R10: 10k, Resistor_SMD:R_0603_1608Metric, F.Cu at (121.0, 124.6)
- D11, D14, D29, D3, D30, D6, D8, R100, R101, R16, R75, R79, R80, R81, R82, RN4, RN6, RN8, U12, U20: moved to B.Cu
- moved U8 140.7 mm to (80.1, 97.8), turned to -90 degrees
- moved J14 139.9 mm to (78.5, 106.9)
- moved D29 132.0 mm to (97.0, 66.3), turned to 90 degrees
- moved D30 130.9 mm to (99.5, 66.3), turned to 90 degrees
- moved U15 122.6 mm to (86.2, 121.0), turned to 180 degrees
- moved U18 121.7 mm to (101.2, 77.8), turned to 90 degrees
- moved D3 112.5 mm to (126.0, 75.1), turned to -90 degrees
- moved U21 112.5 mm to (86.0, 115.0)
- moved RN6 111.8 mm to (111.9, 65.0), turned to -90 degrees
- moved D6 110.8 mm to (128.0, 75.2), turned to -90 degrees
- moved D8 109.2 mm to (130.0, 75.2), turned to -90 degrees
- moved D11 107.6 mm to (132.1, 75.2), turned to -90 degrees
- moved U10 102.6 mm to (90.4, 114.7), turned to 90 degrees
- moved RN1 102.2 mm to (137.8, 75.0), turned to -90 degrees
- moved D10 99.7 mm to (133.8, 97.6), turned to -90 degrees
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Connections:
- C19 pad 1: Net-(RN4-R1.2) -> Net-(RN4-R4.1)
- C25 pad 1: Net-(RN4-R2.2) -> Net-(RN4-R3.1)
- C58 pad 1: Net-(RN4-R3.2) -> Net-(RN4-R2.1)
- C60 pad 1: Net-(RN4-R4.2) -> Net-(RN4-R1.1)
- D14 pad 1: Net-(RN4-R4.2) -> Net-(RN4-R1.1)
- D14 pad 3: Net-(RN4-R3.2) -> Net-(RN4-R2.1)
- D14 pad 4: Net-(RN4-R2.2) -> Net-(RN4-R3.1)
- D14 pad 6: Net-(RN4-R1.2) -> Net-(RN4-R4.1)
- J1 pad 19: MAP_Sensor -> TPS_Sensor
- J1 pad 20: TPS_Sensor -> MAP_Sensor
- J1 pad 4: BOOST-OUT -> IDLE-OUT
- J1 pad 8: IDLE-OUT -> BOOST-OUT
- R79 pad 2: Net-(U23B--) -> Net-(U23A--)
- R80 pad 2: Net-(U23A--) -> Net-(U23B--)
- RN1 pad 1: Net-(D1-A) -> IGN-4-OUT
- RN1 pad 2: Net-(D4-A) -> IGN-3-OUT
- RN1 pad 3: Net-(D9-A) -> IGN-2-OUT
- RN1 pad 4: Net-(D12-A) -> IGN-1-OUT
- RN1 pad 5: IGN-1-OUT -> Net-(D12-A)
- RN1 pad 6: IGN-2-OUT -> Net-(D9-A)
- RN1 pad 7: IGN-3-OUT -> Net-(D4-A)
- RN1 pad 8: IGN-4-OUT -> Net-(D1-A)
- RN4 pad 1: CLT_Sensor -> Net-(RN4-R1.1)
- RN4 pad 2: IAT_Sensor -> Net-(RN4-R2.1)
- RN4 pad 3: TPS_Sensor -> Net-(RN4-R3.1)
- RN4 pad 4: MAP_Sensor -> Net-(RN4-R4.1)
- RN4 pad 5: Net-(RN4-R4.2) -> CLT_Sensor
- RN4 pad 6: Net-(RN4-R3.2) -> IAT_Sensor
- RN4 pad 7: Net-(RN4-R2.2) -> TPS_Sensor
- RN4 pad 8: Net-(RN4-R1.2) -> MAP_Sensor
- RN8 pad 1: GND -> /MAP
- RN8 pad 2: GND -> /TPS
- RN8 pad 3: GND -> /IAT
- RN8 pad 4: GND -> /CLT
- RN8 pad 5: /CLT -> GND
- RN8 pad 6: /IAT -> GND
- RN8 pad 7: /TPS -> GND
- RN8 pad 8: /MAP -> GND
- U23 pad 10: Net-(RN4-R4.2) -> Net-(RN4-R1.1)
- U23 pad 12: Net-(RN4-R3.2) -> Net-(RN4-R2.1)
- U23 pad 3: Net-(RN4-R2.2) -> Net-(RN4-R4.1)
- U23 pad 5: Net-(RN4-R1.2) -> Net-(RN4-R3.1)
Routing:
- net +5C: track 0.00 -> 87.4 mm, vias 0 -> 3
- net CAN+: track 0.00 -> 36.8 mm, vias 0 -> 1
- net INJ-1-OUT: track 0.00 -> 35.5 mm
- net CAN-: track 0.00 -> 34.0 mm, vias 0 -> 1
- net IGN-4-OUT: track 0.00 -> 33.2 mm
- net INJ-2-OUT: track 0.00 -> 32.0 mm
- net Net-(D2-K): track 0.00 -> 31.8 mm, vias 0 -> 1
- net Net-(D1-A): track 0.00 -> 30.8 mm
- net Net-(D4-A): track 0.00 -> 29.0 mm
- net IGN-3-OUT: track 0.00 -> 28.6 mm
- net Net-(D5-K): track 0.00 -> 28.2 mm, vias 0 -> 1
- net HEATER+: track 58.9 -> 86.8 mm, vias 0 -> 2
- net Net-(D9-A): track 0.00 -> 27.2 mm
- net Net-(D12-A): track 0.00 -> 26.3 mm
- net INJ-3-OUT: track 0.00 -> 25.9 mm
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- added copper zone on B.Cu, net GND
- added copper zone on F.Cu, net GND
- added copper zone on In1.Cu, net GND
- added copper zone on In2.Cu, net GND
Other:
- board text added: "Encendido"
- board text added: "Inyección"

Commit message: wip analog frontend & power
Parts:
- C51, C52, C53, C54, U25, U26: moved to B.Cu
- moved U25 122.8 mm to (100.0, 84.0), turned to -90 degrees
- moved U26 120.6 mm to (102.9, 84.0), turned to -90 degrees
- moved RN7 118.6 mm to (101.3, 83.8), turned to 90 degrees
- moved C54 111.5 mm to (100.3, 77.3), turned to 180 degrees
- moved C52 111.2 mm to (100.3, 75.7), turned to 180 degrees
- moved C53 111.0 mm to (100.3, 80.4), turned to 180 degrees
- moved C51 110.9 mm to (100.3, 78.8), turned to 180 degrees
- moved R80 0.25 mm to (104.1, 71.1)
- moved RN8 0.23 mm to (106.2, 74.7), turned to 90 degrees
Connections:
- RN7 pad 5: SW_USER -> SW_AC
- RN7 pad 6: SW_TABLE -> SW_SHIFT
- RN7 pad 7: SW_SHIFT -> SW_TABLE
- RN7 pad 8: SW_AC -> SW_USER
- RN8 pad 1: /MAP -> GND
- RN8 pad 2: /TPS -> GND
- RN8 pad 3: /IAT -> GND
- RN8 pad 4: /CLT -> GND
- RN8 pad 5: GND -> /CLT
- RN8 pad 6: GND -> /IAT
- RN8 pad 7: GND -> /TPS
- RN8 pad 8: GND -> /MAP
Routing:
- net SW_USER: track 0.00 -> 40.6 mm, vias 0 -> 1
- net SW_TABLE: track 0.00 -> 36.4 mm, vias 0 -> 2
- net SW_SHIFT: track 0.00 -> 32.4 mm, vias 0 -> 2
- net SW_AC: track 0.00 -> 31.4 mm, vias 0 -> 2
- net O2_Sensor: track 0.36 -> 12.6 mm
- net GND: track 7.45 -> 12.5 mm, vias 7 -> 8
- net /CLT: track 0.00 -> 3.31 mm
- net /IAT: track 0.00 -> 2.86 mm
- net /TPS: track 0.00 -> 2.15 mm
- net /MAP: track 0.00 -> 1.94 mm
- net Net-(U18-IN2): track 0.00 -> 0.78 mm, vias 0 -> 1
- net IGN-3-OUT: track 28.6 -> 28.0 mm
